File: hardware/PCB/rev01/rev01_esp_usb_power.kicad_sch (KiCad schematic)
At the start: 36 parts, among them J4 USB_C_Receptacle_USB2.0_16P, Q4 DMG3415U, SW1 RESET, SW2 BOOT, U2 ESP32-S3-WROOM-1, U4 MAX17048G+T10, U6 MCP73831T-2ACI/OT, U7 AP2112K-3.3, U8 USBLC6-2P6

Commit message: pcb progress
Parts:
- removed C18: 100n_FG_VDD, Capacitor_SMD:C_0402_1005Metric, symbol Device:C
- removed R10: 10k_ALRT_PU, Resistor_SMD:R_0402_1005Metric, symbol Device:R
- removed R11: 0R_QSTRT_GND, Resistor_SMD:R_0402_1005Metric, symbol Device:R
- added C14: 1uF 16v, Capacitor_SMD:C_0603_1608Metric, symbol Device:C_Small
- added C30: 100n_FG_VDD, Capacitor_SMD:C_0603_1608Metric, symbol Device:C
- added C31: 100nF, Capacitor_SMD:C_0603_1608Metric, symbol Device:C_Small
- added FB17, FB18: Murata BLM18PG121SN1D, Resistor_SMD:R_0603_1608Metric, symbol Device:FerriteBead_Small
- C19, C20, C23, C24: footprint Capacitor_SMD:C_0603_1608Metric -> Capacitor_SMD:C_0805_2012Metric
- C21, C25: footprint Capacitor_SMD:C_0402_1005Metric -> Capacitor_SMD:C_0603_1608Metric
- C22: footprint Capacitor_SMD:C_0805_2012Metric -> Capacitor_SMD:C_0603_1608Metric
- Q4: footprint Package_TO_SOT_SMD:SOT-23 -> PAKT_Local_Fp:SOT-23_GSD
- R12, R13, R14, R15, R16, R19, R21, R3, R4: footprint Resistor_SMD:R_0402_1005Metric -> Resistor_SMD:R_0603_1608Metric
- U4: footprint PAKT_MAX17048_Fp:DFN-8-1EP_3x2mm_P0.5mm_EP1.7x1.4mm -> PAKT_MAX17048_Fp:MAX17048; symbol PAKT_MAX17048_Sym:MAX17048 -> PAKT_MAX17048_Sym:MAX17048G+T10
- U8: footprint USBLC6_2P6 - Copy:USBLC6-2P6 -> Package_TO_SOT_SMD:SOT-666
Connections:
- net GND: now also U4.1 (CTG), U4.4 (GND), U4.6 (QSTRT), C14.2, C30.2, C31.1, FB17.2; no longer J4.A1 (GND), J4.A12 (GND), J4.B1 (GND), J4.B12 (GND), R15.2, R16.2
- net VBAT: now also U4.3 (VDD), C30.1; no longer U4.1 (VDD)
- net VBUS: now also C14.1, FB18.2; no longer C19.1, J4.A4 (VBUS), J4.A9 (VBUS), J4.B4 (VBUS), J4.B9 (VBUS)
- net GND USB OUT: now reaches J4.S1 (SHIELD)
- net GND USB OUT: now also J4.A1 (GND), J4.A12 (GND), J4.B1 (GND), J4.B12 (GND), R15.2, R16.2, C31.2, FB17.1
- net at D5.1 (K), U6.4 (VDD): now also C19.1
- new net USB_IN_POWER: FB18.1, J4.A4 (VBUS), J4.A9 (VBUS), J4.B4 (VBUS), J4.B9 (VBUS)
- no-connect marks 2 -> 24
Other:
- moved on the sheet: BT2, C19, C20, C23, C24, C25, D1, D5, D6, Q4, R12, R13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

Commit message: progress on pcb
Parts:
- added S1: JS102011SAQN, PAKT_Local_Fp:SW_JS102011SAQN, symbol PAKT_SW_JS102011SAQN_Sym:JS102011SAQN
- added SW3: RIGHT, Button_Switch_SMD:SW_SPST_TL3342, symbol Switch:SW_Push
- added SW4: OK, Button_Switch_SMD:SW_SPST_TL3342, symbol Switch:SW_Push
- added SW5: Left, Button_Switch_SMD:SW_SPST_TL3342, symbol Switch:SW_Push
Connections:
- net VBAT: now also S1.2; no longer Q4.D
- new net VBAT_SWITCHED: Q4.D, S1.3
- no-connect marks 24 -> 25

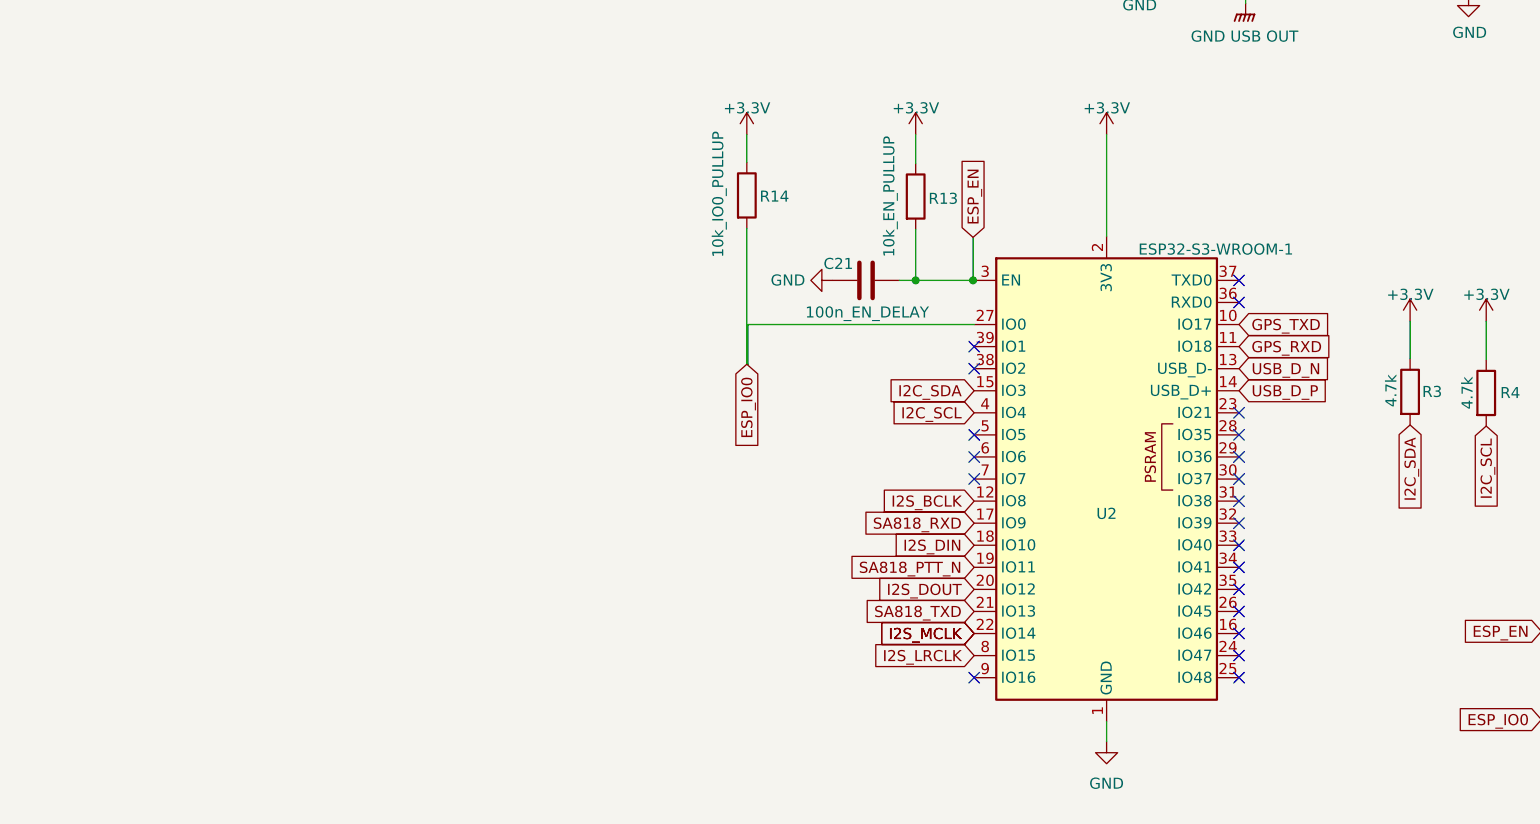
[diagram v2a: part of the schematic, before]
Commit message: added e-paper display
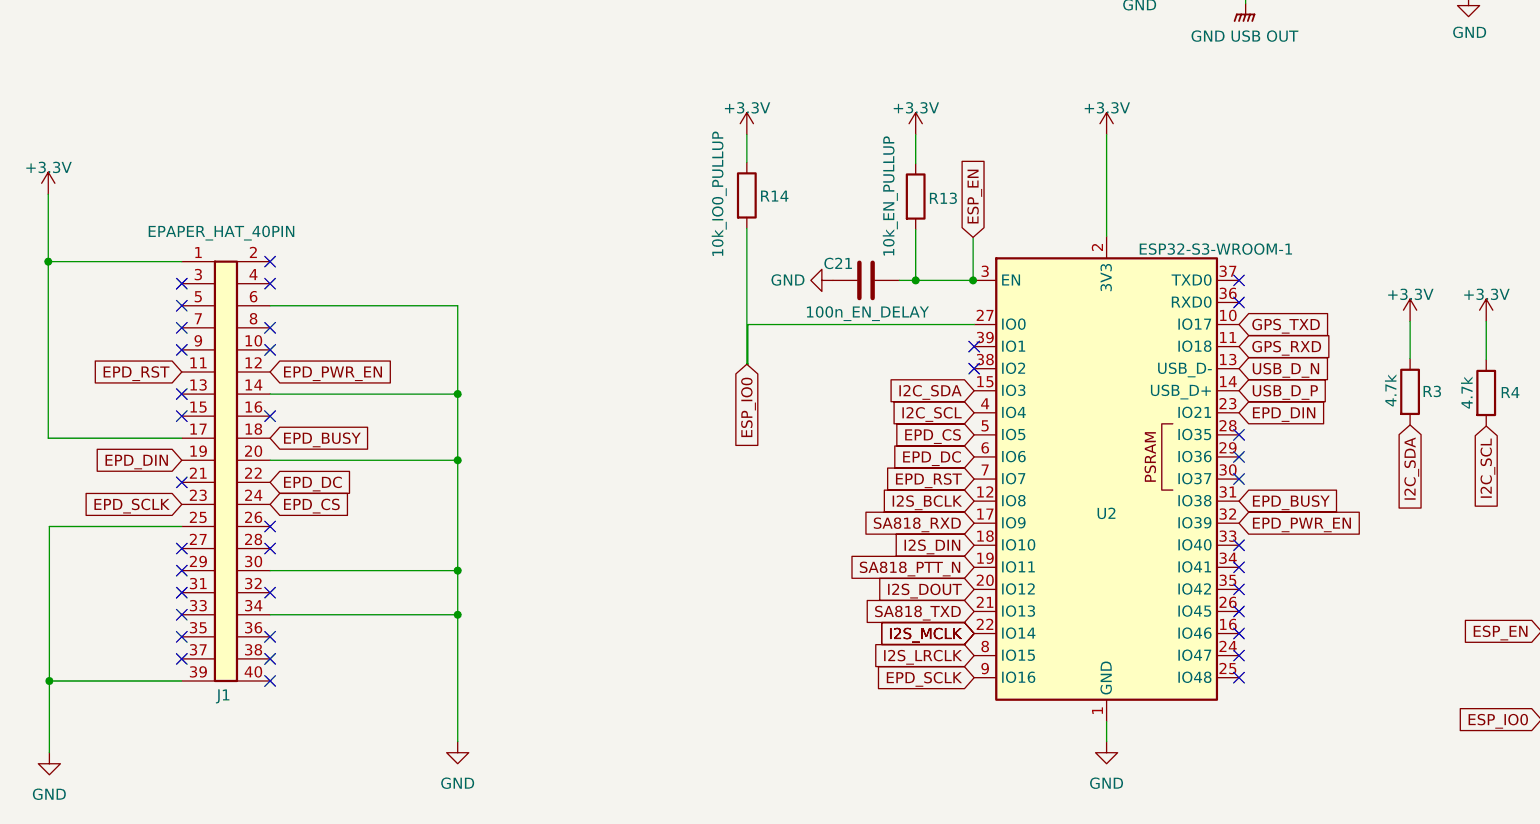
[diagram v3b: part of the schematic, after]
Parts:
- added J1: EPAPER_HAT_40PIN, Connector_PinSocket_2.54mm:PinSocket_2x20_P2.54mm_Vertical, symbol Connector_Generic:Conn_02x20_Odd_Even
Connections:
- net +3.3V: now also J1.1 (Pin_1), J1.17 (Pin_17)
- net GND: now also J1.14 (Pin_14), J1.20 (Pin_20), J1.25 (Pin_25), J1.30 (Pin_30), J1.34 (Pin_34), J1.39 (Pin_39), J1.6 (Pin_6)
- net EPD_DIN: now reaches U2.23 (IO21)
- net EPD_DIN: now also J1.19 (Pin_19)
- net EPD_BUSY: now reaches U2.31 (IO38)
- net EPD_BUSY: now also J1.18 (Pin_18)
- net EPD_PWR_EN: now reaches U2.32 (IO39)
- net EPD_PWR_EN: now also J1.12 (Pin_12)
- net EPD_CS: now reaches U2.5 (IO5)
- net EPD_CS: now also J1.24 (Pin_24)
- net EPD_DC: now reaches U2.6 (IO6)
- net EPD_DC: now also J1.22 (Pin_22)
- net EPD_RST: now reaches U2.7 (IO7)
- net EPD_RST: now also J1.11 (Pin_11)
- net EPD_SCLK: now reaches U2.9 (IO16)
- net EPD_SCLK: now also J1.23 (Pin_23)
- no-connect marks 25 -> 42
